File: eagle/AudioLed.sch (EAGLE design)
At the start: 39 parts, among them Q1 8/16/20MHz, Q2 CMA-4544PF-W, U1 ATMEGA328, U2 L7805CDT-TR, U4 MAX9814TDFN14

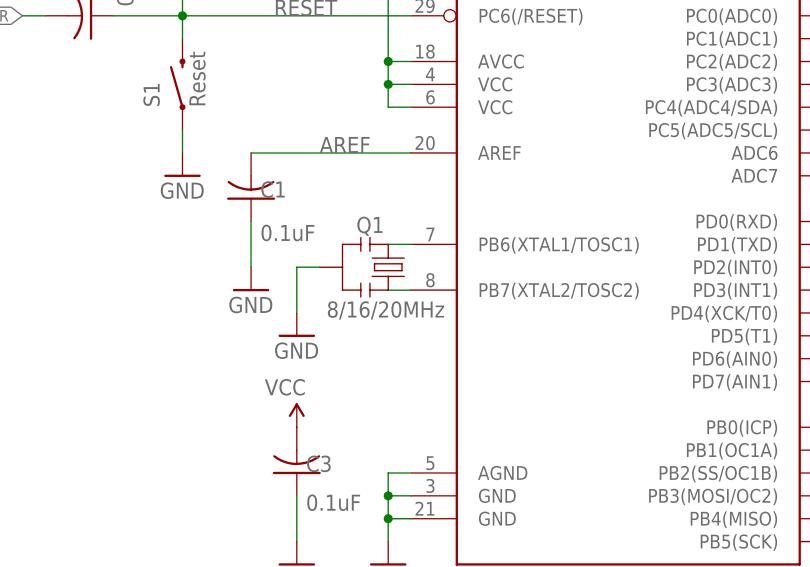
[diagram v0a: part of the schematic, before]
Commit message: Replace bad resonator with SparkFun Resonator
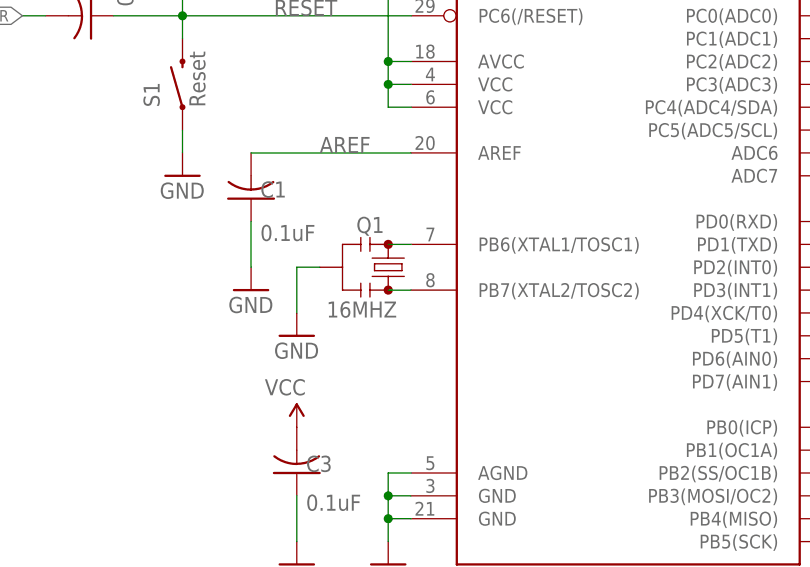
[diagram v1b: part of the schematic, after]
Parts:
- Q1: value 8/16/20MHz -> 16MHZ; device Testing:RESONATOR1:1 -> SparkFun-FreqCtrl:RESONATOR16MHZ
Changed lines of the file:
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@@
 <part name="C2" library="adafruit" deviceset="C-US" device="C0805" value="0.1uF"/>
 <part name="S1" library="Testing" deviceset="SWITCH-MOMENTARY-2" device="SMD-ALT01" value="Reset"/>
-<part name="Q1" library="Testing" deviceset="RESONATOR" device="1:1" value="8/16/20MHz"/>
+<part name="Q1" library="SparkFun-FreqCtrl" deviceset="RESONATOR" device="16MHZ" value="16MHZ"/>
 <part name="U2" library="BAG" deviceset="L7805CDT-TR" device=""/>
 <part name="GND2" library="SparkFun" deviceset="GND" device=""/>
